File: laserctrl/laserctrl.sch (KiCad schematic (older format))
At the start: 13 parts, among them CON1 AVR-ISP-6, IC1 23K256, IC2 ATMEGA328-A, X1 20MHz

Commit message: Deleted the A-axis, it's getting too cramped with limited 328 I/O
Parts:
- gave numbers to parts that had none: 2
- renumbered C47 to C1, C48 to C2, C49 to C3, R33 to R1, R34 to R2, R35 to R3, R36 to R4
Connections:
- wire segments 79 -> 75
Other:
- note removed: "Limit A"
- note removed: "Motor A - STEP"
- note removed: "Motor A - dir"
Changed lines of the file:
@@
-EESchema Schematic File Version 2  date 2011-10-22T12:24:09 CEST
+EESchema Schematic File Version 2  date 2011-10-22T21:04:28 CEST
 LIBS:power
 LIBS:device
@@
 EELAYER END
 $Descr A4 11700 8267
-Sheet 1 6
+Sheet 1 5
 Title ""
 Date "22 oct 2011"
@@
 	6350 2775 6550 2775
 Wire Wire Line
-	6350 4850 6550 4850
-Wire Wire Line
 	6550 2475 6350 2475
 Wire Wire Line
@@
 Wire Wire Line
 	6350 3475 6550 3475
-Wire Wire Line
-	6350 4400 6550 4400
-Wire Wire Line
-	6350 4700 6550 4700
 Wire Wire Line
 	2725 5775 2675 5775
@@
 	2675 5925 2725 5925
 Wire Wire Line
-	6550 4550 6350 4550
-Wire Wire Line
 	6550 3625 6350 3625
 Wire Wire Line
@@
 	1225 3800 1100 3800
 $Comp
-L GND #PWR?
+L GND #PWR1
 U 1 1 4EA297C6
 P 1100 4225
-F 0 "#PWR?" H 1100 4225 30  0001 C CNN
+F 0 "#PWR1" H 1100 4225 30  0001 C CNN
 F 1 "GND" H 1100 4155 30  0001 C CNN
 	1    1100 4225
@@
 TXD
 $Comp
-L CONN_6 P?
+L CONN_6 P1
 U 1 1 4EA29785
 P 1575 3850
-F 0 "P?" V 1525 3850 60  0000 C CNN
+F 0 "P1" V 1525 3850 60  0000 C CNN
 F 1 "CONN_6" V 1625 3850 60  0000 C CNN
 	1    1575 3850
@@
 $EndComp
 $Comp
-L CONN_5 P?
+L CONN_5 P2
 U 1 1 4EA29595
 P 4900 5075
-F 0 "P?" V 4850 5075 50  0000 C CNN
+F 0 "P2" V 4850 5075 50  0000 C CNN
 F 1 "CONN_5" V 4950 5075 50  0000 C CNN
 	1    4900 5075
 	1    0    0    -1
 $EndComp
-Text GLabel 6350 4850 0    50   Input ~ 0
-ADC7
 Text GLabel 6350 3775 0    50   Input ~ 0
-ADC6
+PD7
 Text GLabel 6350 2775 0    50   Input ~ 0
 PD6
 Text GLabel 6350 1800 0    50   Input ~ 0
 PD5
-Text Notes 4850 3150 0    50   ~ 0
-Limit A
-Text Notes 4850 3050 0    50   ~ 0
+Text Notes 4825 4025 0    50   ~ 0
 Limit Z
-Text Notes 4825 4025 0    50   ~ 0
+Text Notes 4825 1925 0    50   ~ 0
 STOP
 Text Notes 4825 3925 0    50   ~ 0
@@
 Text Notes 4825 2425 0    50   ~ 0
 Motor X - DIR
-Text Notes 4825 1925 0    50   ~ 0
-Motor A - STEP
-Text Notes 4825 1825 0    50   ~ 0
-Motor A - dir
 Text Notes 4825 1725 0    50   ~ 0
 Enable motor drivers
-Text GLabel 6350 4700 0    50   Input ~ 0
-PB2
-Text GLabel 6350 4550 0    50   Input ~ 0
-PB1
-Text GLabel 6350 4400 0    50   Input ~ 0
-PB0
 Text GLabel 6350 3325 0    50   Input ~ 0
 PB0
@@
 Text GLabel 6350 1500 0    50   Input ~ 0
 PC0
-$Sheet
-S 6550 4225 700  850
-U 4EA1F594
-F0 "driver-A" 60
-F1 "driver.sch" 60
-F2 "DIR" I L 6550 4550 60
-F3 "STEP" I L 6550 4700 60
-F4 "~ENABLE" I L 6550 4400 60
-F5 "Limit" I L 6550 4850 60
-$EndSheet
 $Sheet
 S 6550 3150 700  825
@@
 $EndSheet
 $Comp
-L R R35
+L R R3
 U 1 1 4EA1C995
 P 2425 5925
-F 0 "R35" V 2505 5925 50  0000 C CNN
+F 0 "R3" V 2505 5925 50  0000 C CNN
 F 1 "200R" V 2425 5925 50  0000 C CNN
 	1    2425 5925
@@
 $EndComp
 $Comp
-L R R34
+L R R2
 U 1 1 4EA1C98F
 P 2425 5775
-F 0 "R34" V 2505 5775 50  0000 C CNN
+F 0 "R2" V 2505 5775 50  0000 C CNN
 F 1 "200R" V 2425 5775 50  0000 C CNN
 	1    2425 5775
@@
 $EndComp
 $Comp
-L R R33
+L R R1
 U 1 1 4EA1C97E
 P 2425 5625
-F 0 "R33" V 2505 5625 50  0000 C CNN
+F 0 "R1" V 2505 5625 50  0000 C CNN
 F 1 "200R" V 2425 5625 50  0000 C CNN
 	1    2425 5625
@@
 $EndComp
 $Comp
-L GND #PWR4
+L GND #PWR5
 U 1 1 4EA1C962
 P 1675 6225
-F 0 "#PWR4" H 1675 6225 30  0001 C CNN
+F 0 "#PWR5" H 1675 6225 30  0001 C CNN
 F 1 "GND" H 1675 6155 30  0001 C CNN
 	1    1675 6225
@@
 $EndComp
 $Comp
-L +3.3V #PWR1
+L +3.3V #PWR2
 U 1 1 4EA1C8DE
 P 1225 5675
-F 0 "#PWR1" H 1225 5635 30  0001 C CNN
+F 0 "#PWR2" H 1225 5635 30  0001 C CNN
 F 1 "+3.3V" H 1225 5785 30  0000 C CNN
 	1    1225 5675
@@
 $EndComp
 $Comp
-L +3.3V #PWR3
+L +3.3V #PWR4
 U 1 1 4EA1C8CD
 P 1675 5350
-F 0 "#PWR3" H 1675 5310 30  0001 C CNN
+F 0 "#PWR4" H 1675 5310 30  0001 C CNN
 F 1 "+3.3V" H 1675 5460 30  0000 C CNN
 	1    1675 5350
@@
 $EndComp
 $Comp
-L GND #PWR7
+L GND #PWR8
 U 1 1 4EA1C108
 P 2200 5100
-F 0 "#PWR7" H 2200 5100 30  0001 C CNN
+F 0 "#PWR8" H 2200 5100 30  0001 C CNN
 F 1 "GND" H 2200 5030 30  0001 C CNN
 	1    2200 5100
@@
 $EndComp
 $Comp
-L +5V #PWR6
+L +5V #PWR7
 U 1 1 4EA1C100
 P 2200 4600
-F 0 "#PWR6" H 2200 4690 20  0001 C CNN
+F 0 "#PWR7" H 2200 4690 20  0001 C CNN
 F 1 "+5V" H 2200 4690 30  0000 C CNN
 	1    2200 4600
@@
 RXD
 $Comp
-L GND #PWR5
+L GND #PWR6
 U 1 1 4EA1B8D4
 P 2050 3000
-F 0 "#PWR5" H 2050 3000 30  0001 C CNN
+F 0 "#PWR6" H 2050 3000 30  0001 C CNN
 F 1 "GND" H 2050 2930 30  0001 C CNN
 	1    2050 3000
@@
 $EndComp
 $Comp
-L GND #PWR2
+L GND #PWR3
 U 1 1 4EA1B8D0
 P 1450 3000
-F 0 "#PWR2" H 1450 3000 30  0001 C CNN
+F 0 "#PWR3" H 1450 3000 30  0001 C CNN
 F 1 "GND" H 1450 2930 30  0001 C CNN
 	1    1450 3000
@@
 $EndComp
 $Comp
-L C C48
+L C C2
 U 1 1 4EA1B8C4
 P 2050 2700
-F 0 "C48" H 2100 2800 50  0000 L CNN
+F 0 "C2" H 2100 2800 50  0000 L CNN
 F 1 "15pF" H 2100 2600 50  0000 L CNN
 	1    2050 2700
@@
 $EndComp
 $Comp
-L C C47
+L C C1
 U 1 1 4EA1B8BB
 P 1450 2700
-F 0 "C47" H 1500 2800 50  0000 L CNN
+F 0 "C1" H 1500 2800 50  0000 L CNN
 F 1 "15pF" H 1500 2600 50  0000 L CNN
 	1    1450 2700
@@
 ~Reset
 $Comp
-L +5V #PWR8
+L +5V #PWR9
 U 1 1 4EA1B75C
 P 2450 2650
-F 0 "#PWR8" H 2450 2740 20  0001 C CNN
+F 0 "#PWR9" H 2450 2740 20  0001 C CNN
 F 1 "+5V" H 2450 2740 30  0000 C CNN
 	1    2450 2650
@@
 $EndComp
 $Comp
-L R R36
+L R R4
 U 1 1 4EA1B741
 P 2450 3000
-F 0 "R36" V 2530 3000 50  0000 C CNN
+F 0 "R4" V 2530 3000 50  0000 C CNN
 F 1 "10k" V 2450 3000 50  0000 C CNN
 	1    2450 3000
@@
 $EndComp
 $Comp
-L GND #PWR9
+L GND #PWR10
 U 1 1 4EA1B73A
 P 2450 4100
-F 0 "#PWR9" H 2450 4100 30  0001 C CNN
+F 0 "#PWR10" H 2450 4100 30  0001 C CNN
 F 1 "GND" H 2450 4030 30  0001 C CNN
 	1    2450 4100
@@
 $EndComp
 $Comp
-L C C49
+L C C3
 U 1 1 4EA1B731
 P 2450 3750
-F 0 "C49" H 2500 3850 50  0000 L CNN
+F 0 "C3" H 2500 3850 50  0000 L CNN
 F 1 "100nF" H 2500 3650 50  0000 L CNN
 	1    2450 3750
@@
 $EndComp
 $Comp
-L GND #PWR11
+L GND #PWR12
 U 1 1 4EA1B63A
 P 3200 4450
-F 0 "#PWR11" H 3200 4450 30  0001 C CNN
+F 0 "#PWR12" H 3200 4450 30  0001 C CNN
 F 1 "GND" H 3200 4380 30  0001 C CNN
 	1    3200 4450
@@
 $EndComp
 $Comp
-L +5V #PWR10
+L +5V #PWR11
 U 1 1 4EA1AD2E
 P 3200 1200
-F 0 "#PWR10" H 3200 1290 20  0001 C CNN
+F 0 "#PWR11" H 3200 1290 20  0001 C CNN
 F 1 "+5V" H 3200 1290 30  0000 C CNN
 	1    3200 1200

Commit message: Started work on ARM 32
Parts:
- removed C1, C2: 15pF, symbol C
- removed C3: 100nF, symbol C
- removed CON1: AVR-ISP-6, AVR-ISP-6, symbol AVR-ISP-6
- removed IC1: 23K256, symbol 23K256
- removed IC2: ATMEGA328-A, TQFP32, symbol ATMEGA328-A
- removed P1: CONN_6, symbol CONN_6
- removed R1, R2, R3: 200R, symbol R
- removed R4: 10k, symbol R
- removed X1: 20MHz, symbol CRYSTAL
- added C?: 18pF, symbol C
- added C?: 15pF, symbol C
- added C? (x2): 5pF, symbol C
- added P?: JTAG, symbol CONN_10X2
- added R?: 100k, symbol R
- added R? (x4): 10k, symbol R
- added R? (x2): R, symbol R
- added U?: LPC1769FBD100, symbol LPC1769FBD100
- added X?: 32768Hz, symbol CRYSTAL
- added X?: 12MHz, symbol CRYSTAL
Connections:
- net labels added: +3.3VADC, +BATT, RTCK, TCK, TDI, TDO, TMS, ~RESET, ~TRST
- net labels removed: +5V, ADC6, ADC7, MISO, MOSI, PB1, PB2, PD2, PD3, PD4, RXD, SCK, TXD, ~Reset, ~reset
- wire segments 75 -> 83
- no-connect marks 3 -> 0
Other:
- note removed: "Enable motor drivers"
- note removed: "FTDI serial"
- note removed: "LASER - PWM"
- note removed: "LASER - ~Fire"
- note removed: "Limit X"
- note removed: "Limit Y"
- note removed: "Limit Z"
- note removed: "Motor X - DIR"
- note removed: "Motor X - STEP"
- note removed: "Motor Y - DIR"
- note removed: "Motor Y - STEP"
- note removed: "Motor Z - DIR"
- note removed: "Motor Z - STEP"
- note removed: "RAM ~CS"
- note removed: "STOP"

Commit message: Actually did some work
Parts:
- added C?: 100nF, symbol C
- added R?: R, symbol R
- R? (x2): value R -> 10k
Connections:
- net labels added: USB+, USB-, USB_VBUS
- net labels removed: PB0, PC0, PC1, PC2, PC3, PC4, PC5, PD5, PD6, PD7
- wire segments 83 -> 78
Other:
- moved on the sheet: P?, R?

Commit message: Added laser interface schematic
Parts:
- removed P2: CONN_5, symbol CONN_5
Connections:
- net labels added: P1.19, P1.22, P1.25, P1.27, PWM1, PWM2, PWM3, PWM4, PWM5, PWM6, RXD0, TXD0, ~ISP
- wire segments 78 -> 100
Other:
- note added: "A Current"
- note added: "E-stop"
- note added: "Fire"
- note added: "LASER PWM"
- note added: "LASER Ready"
- note added: "X Current"
- note added: "Y Current"
- note added: "Z Current"
- note added: "~Watchdog Fire"
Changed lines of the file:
@@
-EESchema Schematic File Version 2  date 2011-10-30T14:11:45 CET
+EESchema Schematic File Version 2  date 2011-10-31T20:32:47 CET
 LIBS:power
 LIBS:device
@@
 EELAYER END
 $Descr A4 11700 8267
-Sheet 1 7
+Sheet 1 8
 Title ""
-Date "30 oct 2011"
+Date "31 oct 2011"
 Rev ""
 Comp ""
@@
 Comment4 ""
 $EndDescr
+Text Notes 5100 4600 0    50   ~ 0
+~Watchdog Fire
+Text Notes 5100 4400 0    50   ~ 0
+LASER Ready
+Text Notes 5100 4100 0    50   ~ 0
+E-stop
+Text Notes 5100 3800 0    50   ~ 0
+Fire
+Wire Wire Line
+	4800 4550 4700 4550
+Wire Wire Line
+	8050 3500 8150 3500
+Wire Wire Line
+	8050 3200 8150 3200
+Wire Wire Line
+	4700 4050 4800 4050
+Wire Wire Line
+	8050 3050 8150 3050
+Wire Wire Line
+	10100 2750 10200 2750
+Wire Wire Line
+	10100 5400 10200 5400
+Wire Wire Line
+	4800 4250 4700 4250
+Wire Wire Line
+	4800 3950 4700 3950
+Wire Wire Line
+	4700 3650 4800 3650
+Wire Wire Line
+	1500 2950 1400 2950
 Connection ~ 7650 7000
 Wire Wire Line
@@
 	7500 6950 7500 7000
 Connection ~ 7500 7000
+Wire Wire Line
+	1400 2850 1500 2850
+Wire Wire Line
+	1400 6450 1500 6450
+Wire Wire Line
+	4700 3850 4800 3850
+Wire Wire Line
+	4700 4150 4800 4150
+Wire Wire Line
+	4700 4450 4800 4450
+Wire Wire Line
+	10200 4100 10100 4100
+Wire Wire Line
+	10100 1400 10200 1400
+Wire Wire Line
+	4800 4350 4700 4350
+Wire Wire Line
+	4700 3750 4800 3750
+Wire Wire Line
+	8150 3350 8050 3350
+Wire Wire Line
+	8150 2900 8050 2900
+Text GLabel 4800 4550 2    50   Input ~ 0
+P1.27
+Text GLabel 8050 3500 0    50   Input ~ 0
+P1.27
+Text GLabel 8050 3350 0    50   Input ~ 0
+P1.25
+Text GLabel 8050 3200 0    50   Input ~ 0
+P1.22
+Text GLabel 8050 2900 0    50   Input ~ 0
+P1.19
+Text GLabel 4800 4350 2    50   Input ~ 0
+P1.25
+Text GLabel 4800 4050 2    50   Input ~ 0
+P1.22
+Text GLabel 4800 3750 2    50   Input ~ 0
+P1.19
+$Sheet
+S 8150 2750 950  900
+U 4EAEE920
+F0 "LASER Interface" 60
+F1 "laser.sch" 60
+F2 "~Watchdog Fire" I L 8150 3500 60
+F3 "Fire" I L 8150 2900 60
+F4 "E-stop" O L 8150 3200 60
+F5 "LASER Ready" O L 8150 3350 60
+F6 "Modulation" I L 8150 3050 60
+$EndSheet
+Text GLabel 8050 3050 0    50   Input ~ 0
+PWM5
+Text GLabel 10100 5400 0    50   Input ~ 0
+PWM4
+Text GLabel 10100 4100 0    50   Input ~ 0
+PWM3
+Text GLabel 10100 2750 0    50   Input ~ 0
+PWM2
+Text GLabel 10100 1400 0    50   Input ~ 0
+PWM1
+Text Notes 5100 4300 0    50   ~ 0
+LASER PWM
+Text Notes 5100 4200 0    50   ~ 0
+A Current
+Text Notes 5100 4000 0    50   ~ 0
+Z Current
+Text Notes 5100 3900 0    50   ~ 0
+Y Current
+Text Notes 5100 3700 0    50   ~ 0
+X Current
+Text GLabel 4800 4450 2    50   Input ~ 0
+PWM6
+Text GLabel 4800 4250 2    50   Input ~ 0
+PWM5
+Text GLabel 4800 4150 2    50   Input ~ 0
+PWM4
+Text GLabel 4800 3950 2    50   Input ~ 0
+PWM3
+Text GLabel 4800 3850 2    50   Input ~ 0
+PWM2
+Text GLabel 4800 3650 2    50   Input ~ 0
+PWM1
+Text GLabel 1400 6450 0    50   Input ~ 0
+~ISP
+Text GLabel 1400 2950 0    50   Input ~ 0
+RXD0
+Text GLabel 1400 2850 0    50   Input ~ 0
+TXD0
 $Comp
 L C C?
@@
 F0 "driver-A" 60
 F1 "driver.sch" 60
-F2 "Max-Limit" I L 10200 5550 60
+F2 "Max-Limit" O L 10200 5550 60
 F3 "Current" I L 10200 5400 60
-F4 "Min-Limit" I L 10200 5700 60
+F4 "Min-Limit" O L 10200 5700 60
 F5 "DIR" I L 10200 5100 60
 F6 "STEP" I L 10200 5250 60
@@
 F3 "STEP" I L 10200 2600 60
 F4 "~ENABLE" I L 10200 2300 60
-F5 "Max-Limit" I L 10200 2900 60
+F5 "Max-Limit" O L 10200 2900 60
 F6 "Current" I L 10200 2750 60
-F7 "Min-Limit" I L 10200 3050 60
+F7 "Min-Limit" O L 10200 3050 60
 $EndSheet
 $Comp
@@
 F1 "watchdog.sch" 60
 $EndSheet
-$Comp
-L CONN_5 P2
-U 1 1 4EA29595
-P 6950 1050
-F 0 "P2" V 6900 1050 50  0000 C CNN
-F 1 "CONN_5" V 7000 1050 50  0000 C CNN
-	1    6950 1050
-	1    0    0    -1
-$EndComp
 $Sheet
 S 10200 3500 700  1100
@@
 F3 "STEP" I L 10200 3950 60
 F4 "~ENABLE" I L 10200 3650 60
-F5 "Max-Limit" I L 10200 4250 60
+F5 "Max-Limit" O L 10200 4250 60
 F6 "Current" I L 10200 4100 60
-F7 "Min-Limit" I L 10200 4400 60
+F7 "Min-Limit" O L 10200 4400 60
 $EndSheet
 $Sheet
@@
 F3 "STEP" I L 10200 1100 60
 F4 "~ENABLE" I L 10200 950 60
-F5 "Max-Limit" I L 10200 1550 60
+F5 "Max-Limit" O L 10200 1550 60
 F6 "Current" I L 10200 1400 60
-F7 "Min-Limit" I L 10200 1700 60
+F7 "Min-Limit" O L 10200 1700 60
 $EndSheet
 $Sheet

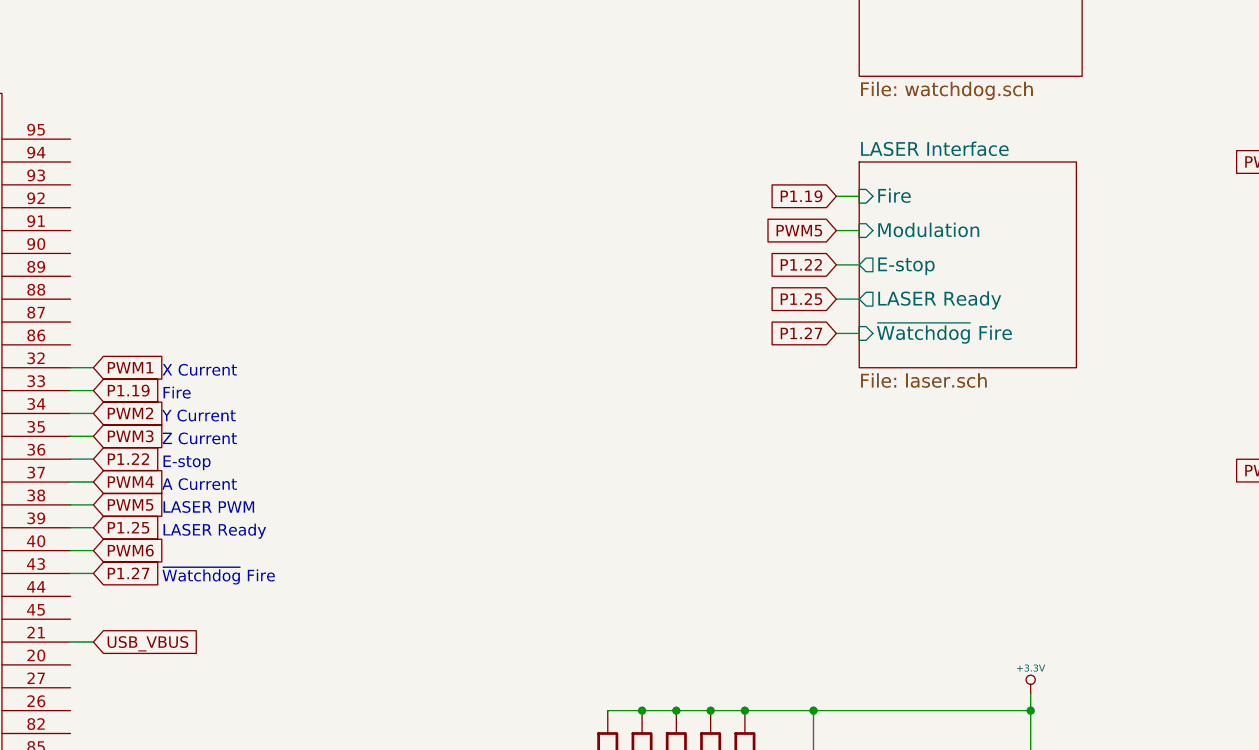
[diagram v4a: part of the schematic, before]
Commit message: Added optocouplers to the LASER interface to protect against induced transients
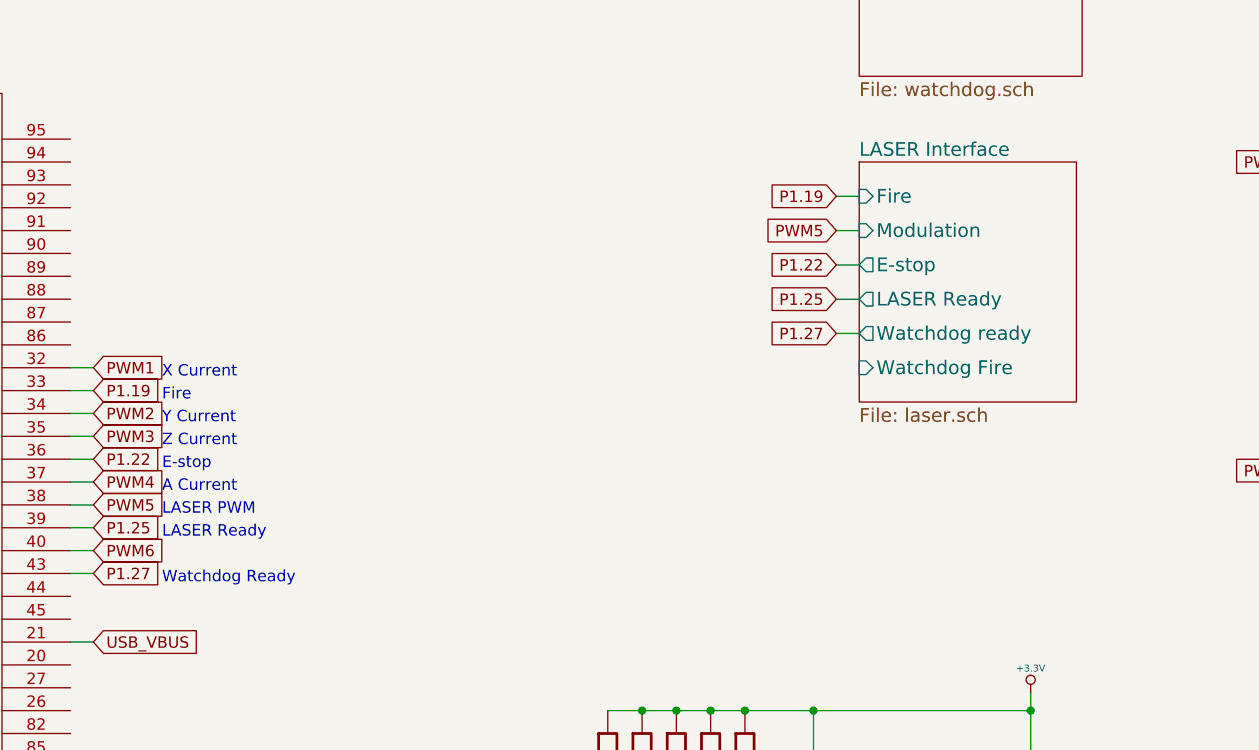
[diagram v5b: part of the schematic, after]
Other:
- note added: "Watchdog Ready"
- note removed: "~Watchdog Fire"
